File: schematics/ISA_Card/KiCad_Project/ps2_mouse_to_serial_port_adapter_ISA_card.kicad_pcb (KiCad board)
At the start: 2 copper layers, 104.2 x 87.9 mm, 19 parts, among them J1 Serial Port, J2 Mini-DIN-6, J3 Bus_ISA_8bit, Q1 BC547, U1 74LS00, U2 L78L05

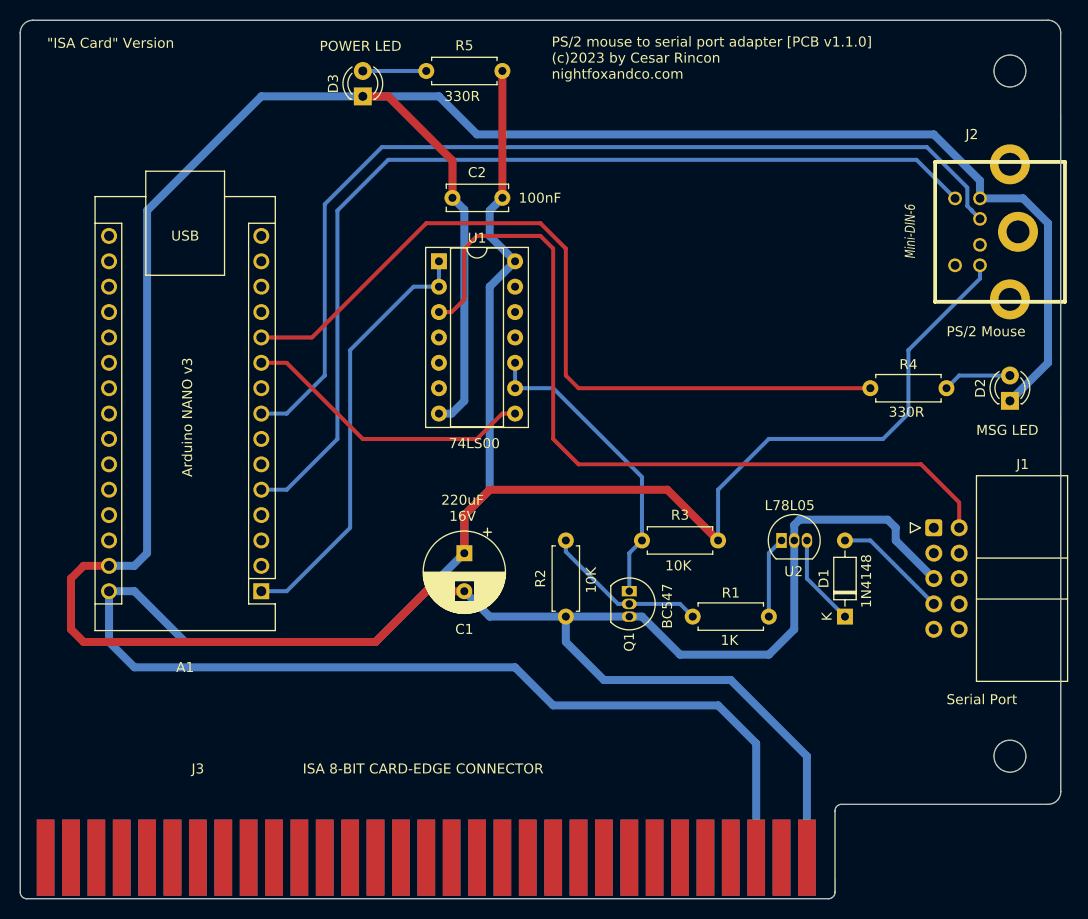
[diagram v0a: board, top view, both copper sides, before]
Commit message: v1.4.0
- Pequeños ajustes al tamaño y contorno de la placa ISA.
- Se han añadido zonas de relleno para GND en la placa ISA.
- Sin cambios en el software.
- Importante! Recordad que aún no he podido verificar en "físico" el diseño de las placas, por lo que recomiendo precaución si van a ser usadas.
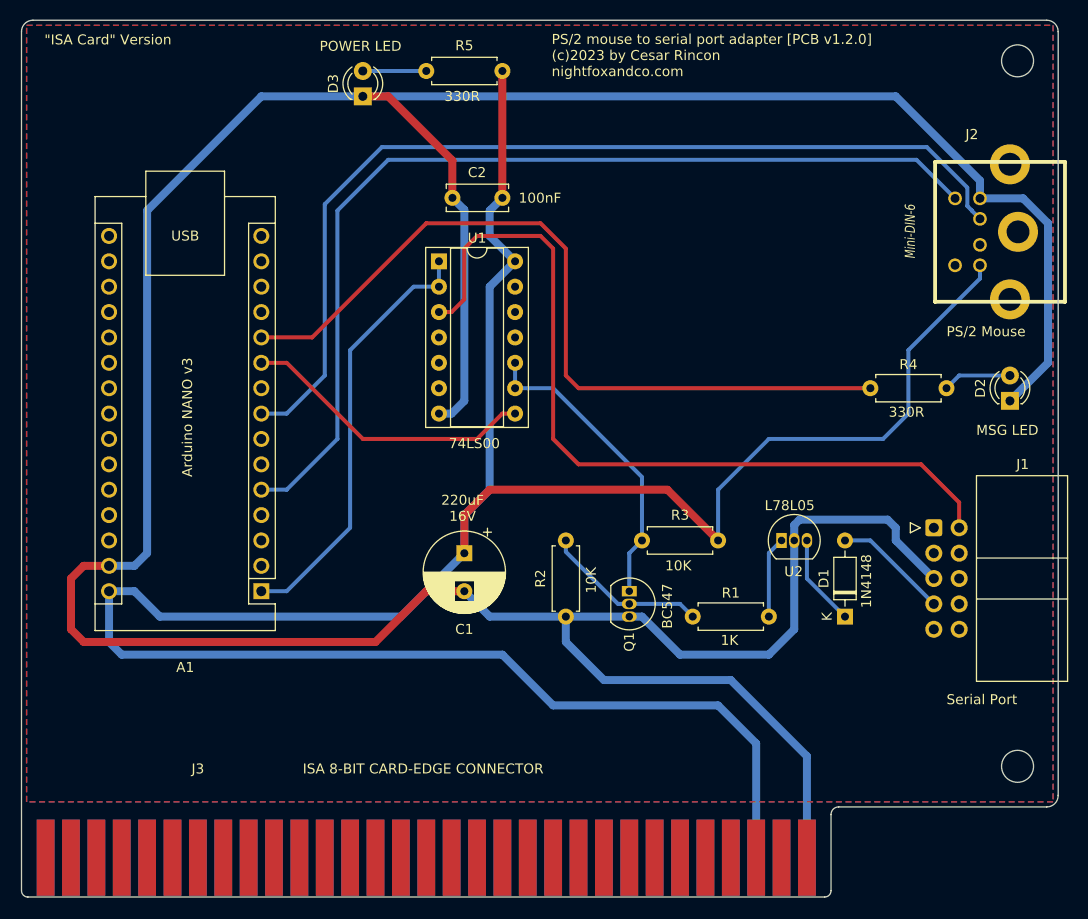
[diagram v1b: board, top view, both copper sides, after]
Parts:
- moved REF** 1.27 mm to (112.5, 87.4)
- moved REF** 1.27 mm to (112.5, 16.8)
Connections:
- net Net-(A1-VIN) renamed /+5V
- net Net-(D2-K) renamed /GND
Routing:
- net /+5V: track 256.2 -> 254.1 mm
- added copper zone on B.Cu, net /GND
- added copper zone on F.Cu, net /GND
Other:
- board size 104.2 x 87.9 mm -> 103.8 x 87.8 mm
- board text added: "PS/2 mouse to serial port adapter [PCB v1.2.0] (c)2023 by Cesar Rincon nightfoxandco.com"
- board text removed: "PS/2 mouse to serial port adapter [PCB v1.1.0] (c)2023 by Cesar Rincon nightfoxandco.com"

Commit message: v1.5.0
- Ajustadas las placas "Stand alone" y "In-a-box" al tamaño standard de
  90x70 mm.
- Añadidas a estas placas las zonas de relleno a masa (GND).
- Añadidas las serigrafias con los valores de todos los componentes en todas
  las versiones de las placas.
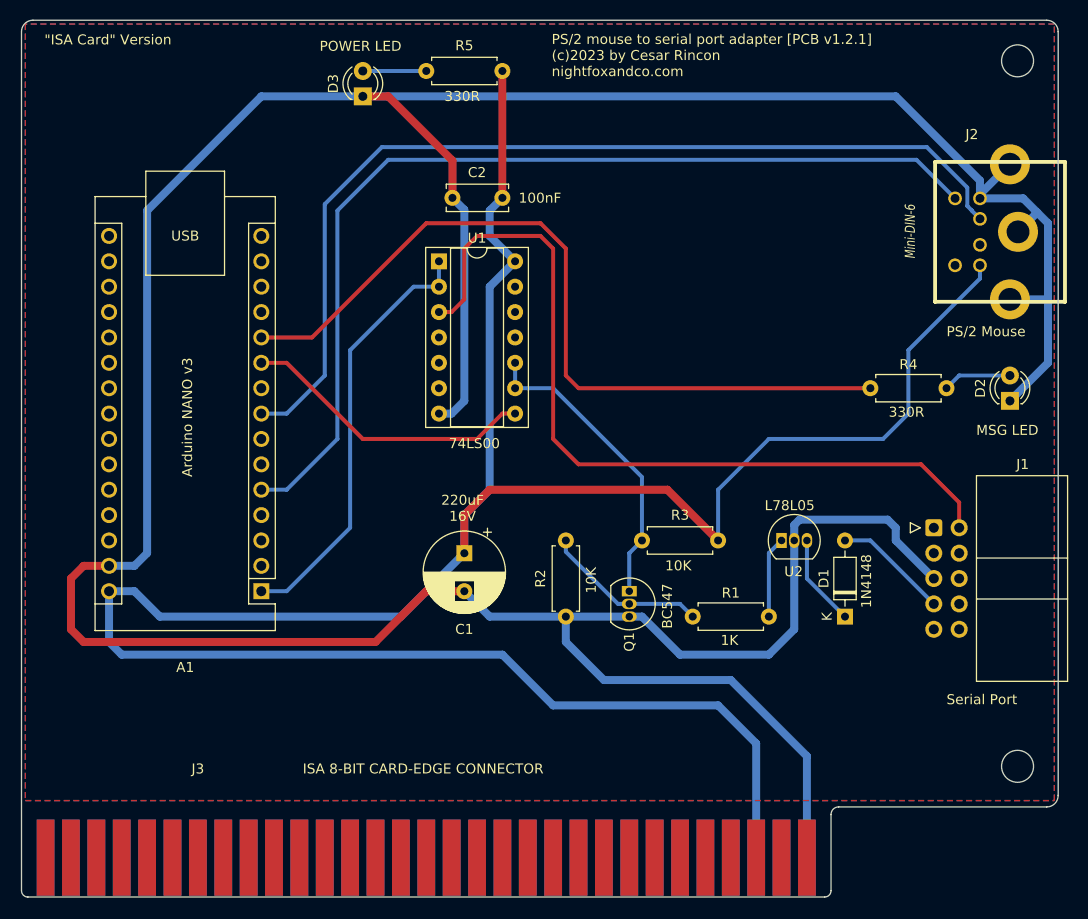
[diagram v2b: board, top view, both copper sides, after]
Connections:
- J2 pad GND: (no net) -> /GND
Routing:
- net /GND: track 355.9 -> 367.1 mm
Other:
- board text added: "PS/2 mouse to serial port adapter [PCB v1.2.1] (c)2023 by Cesar Rincon nightfoxandco.com"
- board text removed: "PS/2 mouse to serial port adapter [PCB v1.2.0] (c)2023 by Cesar Rincon nightfoxandco.com"
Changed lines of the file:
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@@
     (pad "6" thru_hole circle (at 3.35026 11.00074 90) (size 1.3716 1.3716) (drill 0.889) (layers "*.Cu" "*.Mask" "F.SilkS")
       (net 52 "unconnected-(J2-Pad6)") (pintype "passive+no_connect"))
-    (pad "GND" thru_hole circle (at -6.75894 5.50926 90) (size 4.0005 4.0005) (drill 2.29108) (layers "*.Cu" "*.SilkS" "*.Mask"))
-    (pad "GND" thru_hole circle (at 0 4.699 90) (size 4.0005 4.0005) (drill 2.29108) (layers "*.Cu" "*.SilkS" "*.Mask"))
-    (pad "GND" thru_hole circle (at 6.75894 5.50926 90) (size 4.0005 4.0005) (drill 2.29108) (layers "*.Cu" "*.SilkS" "*.Mask"))
+    (pad "GND" thru_hole circle (at -6.75894 5.50926 90) (size 4.0005 4.0005) (drill 2.29108) (layers "*.Cu" "*.SilkS" "*.Mask")
+      (net 1 "/GND"))
+    (pad "GND" thru_hole circle (at 0 4.699 90) (size 4.0005 4.0005) (drill 2.29108) (layers "*.Cu" "*.SilkS" "*.Mask")
+      (net 1 "/GND"))
+    (pad "GND" thru_hole circle (at 6.75894 5.50926 90) (size 4.0005 4.0005) (drill 2.29108) (layers "*.Cu" "*.SilkS" "*.Mask")
+      (net 1 "/GND"))
     (model "r_mini_dins/minidin_6.wrl"
       (offset (xyz 0 0 0))
@@
     (effects (font (size 1 1) (thickness 0.1)) (justify left bottom))
   )
-  (gr_text "PS/2 mouse to serial port adapter [PCB v1.2.0]\n(c)2023 by Cesar Rincon\nnightfoxandco.com" (at 65.887797 18.415) (layer "F.SilkS")
+  (gr_text "PS/2 mouse to serial port adapter [PCB v1.2.1]\n(c)2023 by Cesar Rincon\nnightfoxandco.com" (at 65.887797 18.415) (layer "F.SilkS")
     (effects (font (size 1 1) (thickness 0.1)) (justify left bottom))
   )
@@
   (segment (start 53.34 69.85) (end 48.26 74.93) (width 0.8) (layer "F.Cu") (net 1))
   (segment (start 57.15 69.85) (end 53.34 69.85) (width 0.8) (layer "F.Cu") (net 1))
+  (segment (start 112.57026 33.86074) (end 114.4905 31.9405) (width 0.8) (layer "B.Cu") (net 1))
+  (segment (start 114.4905 31.9405) (end 115.57 33.02) (width 0.8) (layer "B.Cu") (net 1))
   (segment (start 67.31 74.93) (end 67.31 72.39) (width 0.8) (layer "B.Cu") (net 1))
-  (segment (start 115.57 33.02) (end 115.57 46.99) (width 0.8) (layer "B.Cu") (net 1))
   (segment (start 67.31 72.39) (end 73.66 72.39) (width 0.8) (layer "B.Cu") (net 1))
+  (segment (start 112.57026 33.88106) (end 112.57026 33.86074) (width 0.2) (layer "B.Cu") (net 1))
   (segment (start 100.33 64.77) (end 100.33 63.5) (width 0.8) (layer "B.Cu") (net 1))
-  (segment (start 113.0808 30.5308) (end 115.57 33.02) (width 0.8) (layer "B.Cu") (net 1))
   (segment (start 115.57 46.99) (end 111.76 50.8) (width 0.8) (layer "B.Cu") (net 1))
   (segment (start 57.15 69.85) (end 59.69 72.39) (width 0.8) (layer "B.Cu") (net 1))
   (segment (start 90.17 73.66) (end 90.17 64.77) (width 0.8) (layer "B.Cu") (net 1))
+  (segment (start 108.76026 30.12186) (end 108.76026 30.5308) (width 0.2) (layer "B.Cu") (net 1))
   (segment (start 100.33 20.32) (end 46.99 20.32) (width 0.8) (layer "B.Cu") (net 1))
   (segment (start 108.76026 28.75026) (end 100.33 20.32) (width 0.8) (layer "B.Cu") (net 1))
+  (segment (start 113.0808 30.5308) (end 114.4905 31.9405) (width 0.8) (layer "B.Cu") (net 1))
   (segment (start 36.83 20.32) (end 25.4 31.75) (width 0.8) (layer "B.Cu") (net 1))
   (segment (start 59.69 72.39) (end 67.31 72.39) (width 0.8) (layer "B.Cu") (net 1))
@@
   (segment (start 73.66 72.39) (end 74.93 72.39) (width 0.8) (layer "B.Cu") (net 1))
   (segment (start 104.14 68.58) (end 100.33 64.77) (width 0.8) (layer "B.Cu") (net 1))
+  (segment (start 115.57 40.64) (end 115.57 46.99) (width 0.8) (layer "B.Cu") (net 1))
   (segment (start 74.93 72.39) (end 78.74 76.2) (width 0.8) (layer "B.Cu") (net 1))
+  (segment (start 111.76 27.12212) (end 108.76026 30.12186) (width 0.8) (layer "B.Cu") (net 1))
   (segment (start 90.702966 62.687034) (end 90.17 63.22) (width 0.8) (layer "B.Cu") (net 1))
   (segment (start 83.82 78.74) (end 71.12 78.74) (width 0.8) (layer "B.Cu") (net 1))
+  (segment (start 115.57 33.02) (end 115.57 40.64) (width 0.8) (layer "B.Cu") (net 1))
   (segment (start 25.4 66.04) (end 24.13 67.31) (width 0.8) (layer "B.Cu") (net 1))
   (segment (start 108.76026 30.5308) (end 108.76026 28.75026) (width 0.8) (layer "B.Cu") (net 1))
+  (segment (start 111.76 40.64) (end 115.57 40.64) (width 0.8) (layer "B.Cu") (net 1))
   (segment (start 71.12 78.74) (end 67.31 74.93) (width 0.8) (layer "B.Cu") (net 1))
   (segment (start 55.88 52.07) (end 57.15 50.8) (width 0.8) (layer "B.Cu") (net 1))
@@
     (polygon
       (pts
-        (xy 13.335 13.208)
-        (xy 116.078 13.208)
-        (xy 116.078 90.932)
-        (xy 13.335 90.932)
+        (xy 13.208 90.805)
+        (xy 116.205 90.805)
+        (xy 116.205 13.081)
+        (xy 13.208 13.081)
       )
     )

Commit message: v1.5.1
- Arreglada la serigrafía del conector MINI-DIN-6 (PS/2), la cual se superponía en algunas zonas de soldado.
- En todas las placas se añade el símbolo de los agujeros de montaje con el tamaño estándar M3.
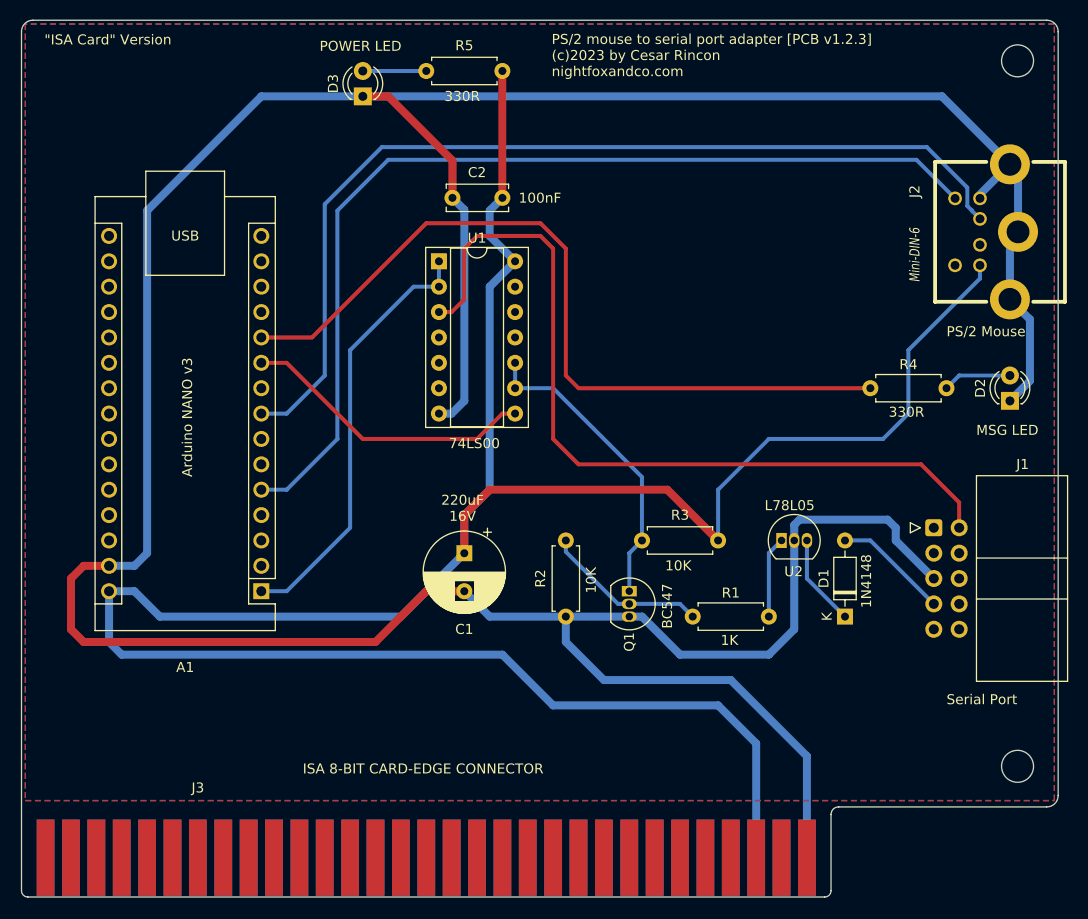
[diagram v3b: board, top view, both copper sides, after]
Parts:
- removed REF** (x2): MountingHole_3.2mm_M3, MountingHole:MountingHole_3.2mm_M3
- added H1: MountingHole, MountingHole:MountingHole_3.2mm_M3, F.Cu at (112.5, 16.8)
- added H2: MountingHole, MountingHole:MountingHole_3.2mm_M3, F.Cu at (112.5, 87.4)
- J2: footprint CustomLib:Conn_Mini_DIN_6pin -> ProjectLibrary:Connector_Mini_DIN_6pin
- J3: footprint CustomLib:BUS_AT -> ProjectLibrary:BUS_AT_ISA_8BITS
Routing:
- net /GND: track 367.1 -> 357.2 mm
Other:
- board text added: "PS/2 mouse to serial port adapter [PCB v1.2.3] (c)2023 by Cesar Rincon nightfoxandco.com"
- board text removed: "PS/2 mouse to serial port adapter [PCB v1.2.1] (c)2023 by Cesar Rincon nightfoxandco.com"

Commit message: v1.7.0
- Modificadas las huellas de todas las placas para que los componentes TO92 resulten más fáciles de soldar a mano.
- Modificadas las conexiones del conector IDC en la placa ISA para poder usar un cable IDC a DB9 comercial, sin necesidad de realizarle modificaciones.
- Añadido el modelo en formato FreeCad y el archivo STL del soporte para la placa ISA. Estos archivos estan preparados para poder realizar la impresión en 3D del soporte. Se recomienda un in-fill del 100%.
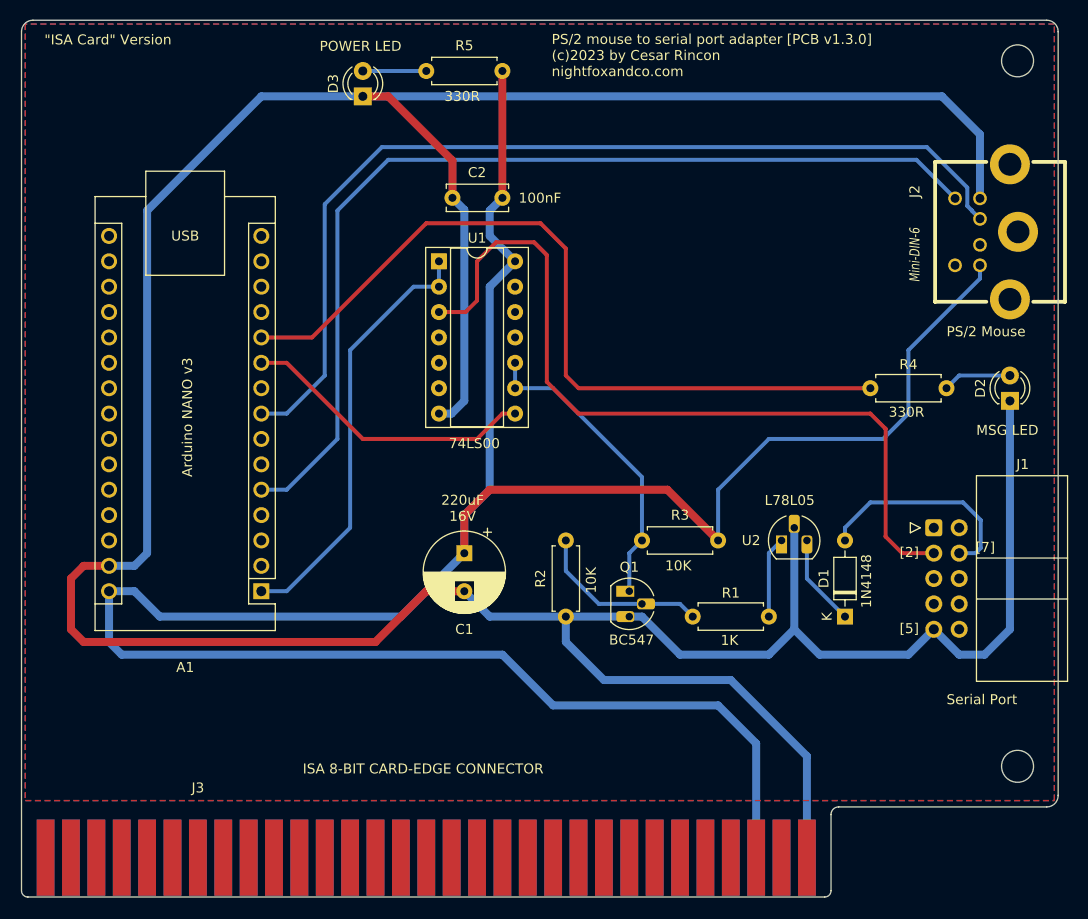
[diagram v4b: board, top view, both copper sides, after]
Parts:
- J1: value Serial Port -> IDC Connector
- Q1, U2: footprint Package_TO_SOT_THT:TO-92_Inline -> Package_TO_SOT_THT:TO-92_HandSolder
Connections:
- J1 pad 2: Net-(J1-Pin_2) -> unconnected-(J1-Pin_2-Pad2)
- J1 pad 3: unconnected-(J1-Pin_3-Pad3) -> Net-(J1-Pin_3)
- J1 pad 4: unconnected-(J1-Pin_4-Pad4) -> Net-(D1-A)
- J1 pad 5: /GND -> unconnected-(J1-Pin_5-Pad5)
- J1 pad 7: Net-(D1-A) -> unconnected-(J1-Pin_7-Pad7)
- J1 pad 9: unconnected-(J1-Pin_9-Pad9) -> /GND
- J2 pad GND: /GND -> (no net)
- U1 pad 3: Net-(J1-Pin_2) -> Net-(J1-Pin_3)
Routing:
- net Net-(J1-Pin_2): track 82.9 -> 0.00 mm
- net Net-(J1-Pin_3): track 0.00 -> 81.4 mm
- net Net-(D1-A): track 11.5 -> 21.8 mm
- net /GND: track 357.2 -> 362.4 mm
- net Net-(Q1-B): track 16.5 -> 17.6 mm
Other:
- board text added: "PS/2 mouse to serial port adapter [PCB v1.3.0] (c)2023 by Cesar Rincon nightfoxandco.com"
- board text added: "[2]"
- board text added: "[5]"
- board text added: "[7]"
- board text removed: "PS/2 mouse to serial port adapter [PCB v1.2.3] (c)2023 by Cesar Rincon nightfoxandco.com"

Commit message: v1.7.1
- Modificado el ancho de la pista de alimentación del puerto PS/2 de la placa ISA.
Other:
- board text added: "PS/2 mouse to serial port adapter [PCB v1.3.1] (c)2023 by Cesar Rincon nightfoxandco.com"
- board text removed: "PS/2 mouse to serial port adapter [PCB v1.3.0] (c)2023 by Cesar Rincon nightfoxandco.com"
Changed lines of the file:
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@@
     (effects (font (size 1 1) (thickness 0.1)) (justify left bottom))
   )
-  (gr_text "PS/2 mouse to serial port adapter [PCB v1.3.0]\n(c)2023 by Cesar Rincon\nnightfoxandco.com" (at 65.887797 18.415) (layer "F.SilkS")
+  (gr_text "PS/2 mouse to serial port adapter [PCB v1.3.1]\n(c)2023 by Cesar Rincon\nnightfoxandco.com" (at 65.887797 18.415) (layer "F.SilkS")
     (effects (font (size 1 1) (thickness 0.1)) (justify left bottom))
   )
@@
   (segment (start 59.69 59.69) (end 77.47 59.69) (width 0.8) (layer "F.Cu") (net 5))
   (segment (start 60.96 30.48) (end 60.96 17.78) (width 0.8) (layer "F.Cu") (net 5))
-  (segment (start 87.63 54.61) (end 82.55 59.69) (width 0.4) (layer "B.Cu") (net 5))
+  (segment (start 87.63 54.61) (end 82.55 59.69) (width 0.8) (layer "B.Cu") (net 5))
   (segment (start 59.69 34.29) (end 59.69 31.75) (width 0.8) (layer "B.Cu") (net 5))
   (segment (start 59.69 31.75) (end 60.96 30.48) (width 0.8) (layer "B.Cu") (net 5))
@@
   (segment (start 62.23 36.83) (end 59.69 39.37) (width 0.8) (layer "B.Cu") (net 5))
   (segment (start 66.04 81.28) (end 82.55 81.28) (width 0.8) (layer "B.Cu") (net 5))
-  (segment (start 101.6 45.72) (end 101.6 52.07) (width 0.4) (layer "B.Cu") (net 5))
+  (segment (start 101.6 45.72) (end 101.6 52.07) (width 0.8) (layer "B.Cu") (net 5))
   (segment (start 86.36 85.09) (end 86.36 96.52) (width 0.8) (layer "B.Cu") (net 5))
   (segment (start 82.55 81.28) (end 86.36 85.09) (width 0.8) (layer "B.Cu") (net 5))
-  (segment (start 99.06 54.61) (end 87.63 54.61) (width 0.4) (layer "B.Cu") (net 5))
+  (segment (start 99.06 54.61) (end 87.63 54.61) (width 0.8) (layer "B.Cu") (net 5))
   (segment (start 60.96 76.2) (end 66.04 81.28) (width 0.8) (layer "B.Cu") (net 5))
   (segment (start 21.59 69.85) (end 21.59 74.93) (width 0.8) (layer "B.Cu") (net 5))
-  (segment (start 108.76026 37.23132) (end 108.76026 38.55974) (width 0.4) (layer "B.Cu") (net 5))
+  (segment (start 108.76026 37.23132) (end 108.76026 38.55974) (width 0.8) (layer "B.Cu") (net 5))
   (segment (start 22.86 76.2) (end 60.96 76.2) (width 0.8) (layer "B.Cu") (net 5))
   (segment (start 21.59 69.85) (end 24.13 69.85) (width 0.8) (layer "B.Cu") (net 5))
   (segment (start 62.23 36.83) (end 59.69 34.29) (width 0.8) (layer "B.Cu") (net 5))
   (segment (start 50.8 72.39) (end 57.14 66.05) (width 0.8) (layer "B.Cu") (net 5))
-  (segment (start 108.76026 38.55974) (end 101.6 45.72) (width 0.4) (layer "B.Cu") (net 5))
-  (segment (start 101.6 52.07) (end 99.06 54.61) (width 0.4) (layer "B.Cu") (net 5))
-  (segment (start 82.55 59.69) (end 82.55 64.77) (width 0.4) (layer "B.Cu") (net 5))
+  (segment (start 108.76026 38.55974) (end 101.6 45.72) (width 0.8) (layer "B.Cu") (net 5))
+  (segment (start 101.6 52.07) (end 99.06 54.61) (width 0.8) (layer "B.Cu") (net 5))
+  (segment (start 82.55 59.69) (end 82.55 64.77) (width 0.8) (layer "B.Cu") (net 5))
   (segment (start 26.67 72.39) (end 50.8 72.39) (width 0.8) (layer "B.Cu") (net 5))
   (segment (start 21.59 74.93) (end 22.86 76.2) (width 0.8) (layer "B.Cu") (net 5))
